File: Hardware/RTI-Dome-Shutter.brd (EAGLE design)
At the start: 80 x 71.1 mm, 42 parts, among them IC1 24AA128ST, IC5 74LVC245, IC6 74ABT245

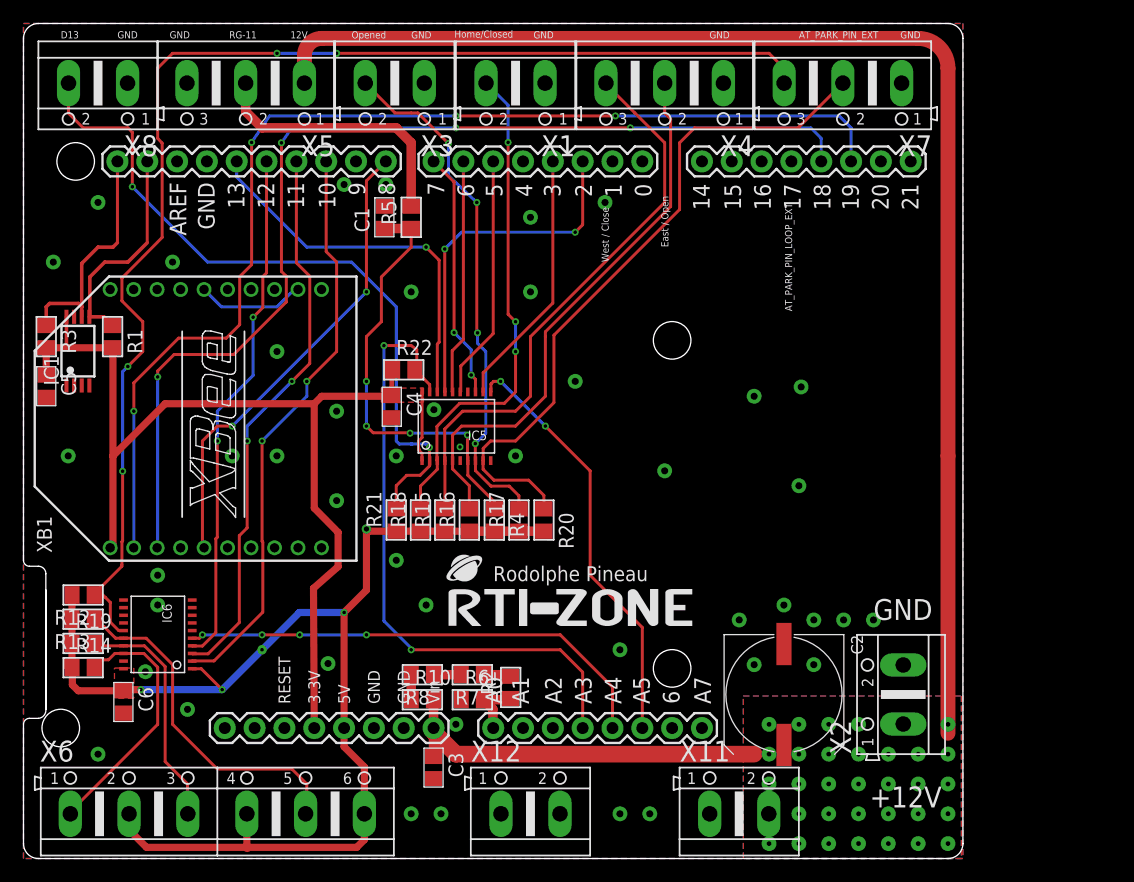
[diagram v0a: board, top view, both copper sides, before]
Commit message: Added powerpole to shutter shield
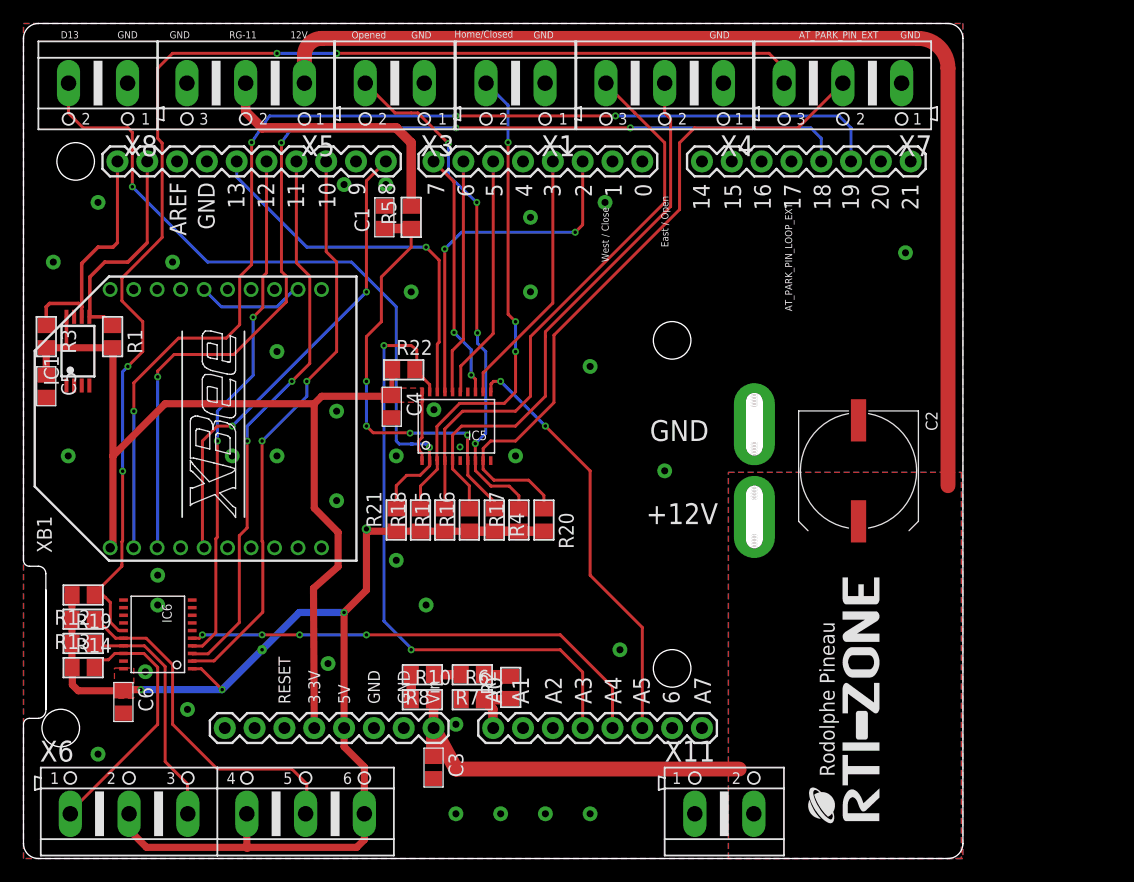
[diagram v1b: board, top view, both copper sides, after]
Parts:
- removed X12, X2: (no value), con-ptr500:AK500/2
- added J1: POWERPOLE_POWER45A, powerpoles:POWERPOLE_PAIR_45A
- moved U$4 40.3 mm to (72.9, 3.17), turned to 90 degrees
- moved C2 20.1 mm to (71.1, 33.0)
- moved X11 1.27 mm to (59.7, 3.81)
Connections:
- net +12V: now also J1.RED; no longer X2.1
- net GND: now also J1.BLACK; no longer X12.1, X12.2, X2.2
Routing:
- net +12V: track 148.7 -> 127.3 mm, vias 32 -> 0

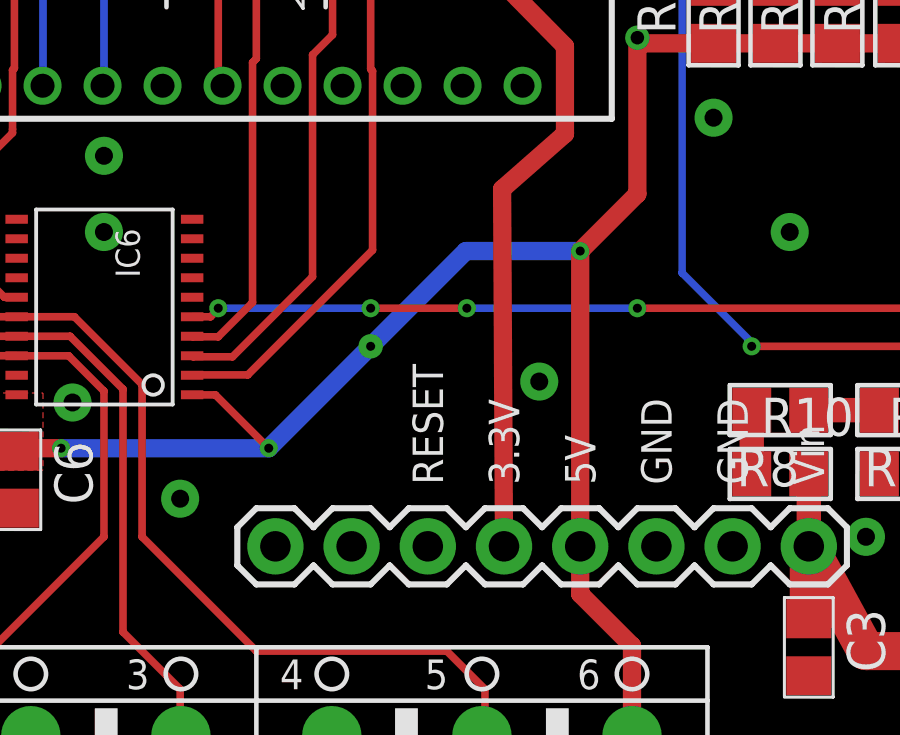
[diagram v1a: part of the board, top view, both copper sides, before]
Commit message: Adding MCP120 for power on reset.
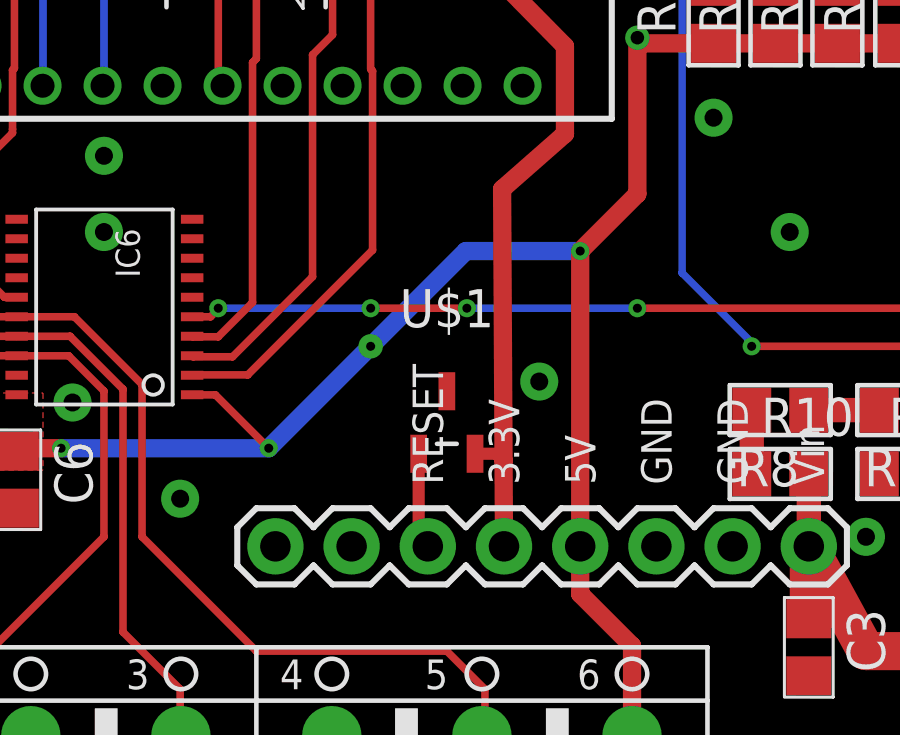
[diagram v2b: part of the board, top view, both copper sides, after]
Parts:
- added U$1: MCP120T-270I_TT, MCP120T-270I_TT:SOT95P237X112-3N
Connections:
- new net RESET: PCB1.RESET, U$1.1
- net 3.3V: now also U$1.2
- net GND: now also U$1.3
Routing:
- net RESET: track 0.00 -> 3.21 mm
- net 3.3V: track 91.5 -> 92.5 mm
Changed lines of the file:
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@@
 <element name="R22" library="rti" package="R0805" value="4.7K" x="32.385" y="41.62425"/>
 <element name="J1" library="powerpoles" package="POWERPOLE_PAIR_45A" value="POWERPOLE_POWER45A" x="62.23" y="33.02" rot="MR90"/>
+<element name="U$1" library="MCP120T-270I_TT" package="SOT95P237X112-3N" value="MCP120T-270I_TT" x="22.86" y="15.24">
+<attribute name="MANUFACTURER_PART_NUMBER" value="MCP120T-270I/TT" x="22.86" y="15.24" size="1.778" layer="27" display="off"/>
+<attribute name="MANUFACTURER_NAME" value="Microchip" x="22.86" y="15.24" size="1.778" layer="27" display="off"/>
+<attribute name="MOUSER_PART_NUMBER" value="579-MCP120T-270I/TT" x="22.86" y="15.24" size="1.778" layer="27" display="off"/>
+<attribute name="DESCRIPTION" value="Microcontroller Supervisory Circuit" x="22.86" y="15.24" size="1.778" layer="27" display="off"/>
+<attribute name="HEIGHT" value="mm" x="22.86" y="15.24" size="1.778" layer="27" display="off"/>
+<attribute name="MOUSER_PRICE-STOCK" value="https://www.mouser.co.uk/ProductDetail/Microchip-Technology/MCP120T-270I-TT?qs=JaP0%252BruNJH91Pwyk6aJdSA%3D%3D" x="22.86" y="15.24" size="1.778" layer="27" display="off"/>
+</element>
 </elements>
 <signals>
@@
 <via x="37.17925" y="35.052" extent="1-16" drill="0.3" diameter="0.254"/>
 <contactref element="J1" pad="BLACK"/>
+<contactref element="U$1" pad="3"/>
 <wire x1="62.25" y1="36.99" x2="62.23" y2="39.37" width="0" layer="19" extent="1-1"/>
 </signal>
@@
 <wire x1="7.62" y1="26.702" x2="7.383" y2="26.465" width="0.6096" layer="1"/>
 <contactref element="PCB1" pad="3.3V"/>
-<wire x1="24.765" y1="11.1125" x2="24.7015" y2="23.01875" width="0.6096" layer="1"/>
+<wire x1="24.765" y1="11.1125" x2="24.74974375" y2="13.97330625" width="0.6096" layer="1"/>
+<wire x1="24.74974375" y1="13.97330625" x2="24.7015" y2="23.01875" width="0.6096" layer="1"/>
 <wire x1="24.7015" y1="23.01875" x2="26.797" y2="24.86025" width="0.6096" layer="1"/>
 <wire x1="26.797" y1="24.86025" x2="26.797" y2="27.78125" width="0.6096" layer="1"/>
@@
 <wire x1="31.435" y1="41.62425" x2="31.369" y2="41.55825" width="0.4064" layer="1"/>
 <wire x1="31.369" y1="41.55825" x2="31.369" y2="39.431" width="0.4064" layer="1"/>
+<contactref element="U$1" pad="2"/>
+<wire x1="23.7998" y1="14.1986" x2="24.52445" y2="14.1986" width="0.4064" layer="1"/>
+<wire x1="24.52445" y1="14.1986" x2="24.74974375" y2="13.97330625" width="0.4064" layer="1"/>
 </signal>
 <signal name="RG-11-IN_5V">
@@
 <contactref element="IC5" pad="P$14"/>
 </signal>
+<signal name="RESET">
+<contactref element="PCB1" pad="RESET"/>
+<contactref element="U$1" pad="1"/>
+<wire x1="21.9202" y1="14.1986" x2="21.9202" y2="11.4173" width="0.4064" layer="1"/>
+<wire x1="21.9202" y1="11.4173" x2="22.225" y2="11.1125" width="0.4064" layer="1"/>
+</signal>
 </signals>

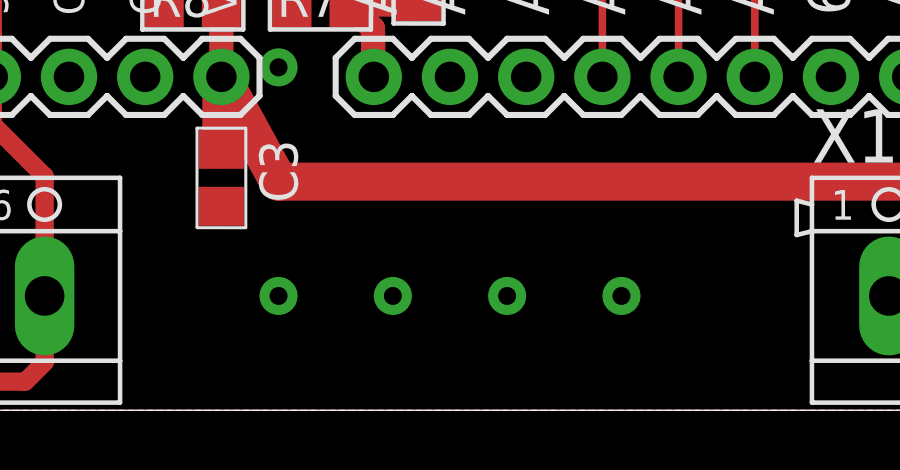
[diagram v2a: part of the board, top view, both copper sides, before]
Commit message: Redid the analog 3.3V on the ethernet shield
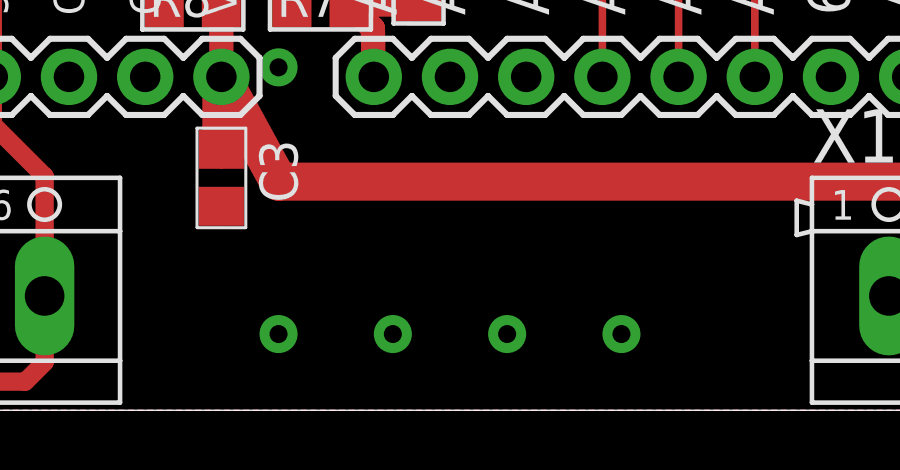
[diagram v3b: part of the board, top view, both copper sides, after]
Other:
- board text added: "Dome Shutter"
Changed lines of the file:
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@@
 <text x="3.175" y="69.85" size="0.6096" layer="21">D13</text>
 <text x="4.60375" y="68.61175" size="0.6096" layer="22" rot="MR0">D13</text>
+<text x="36.83" y="3.81" size="1.778" layer="51">Dome Shutter</text>
 </plain>
 <attributes>
@@
 <via x="6.35" y="8.89" extent="1-16" drill="0.6" diameter="1.27"/>
 <via x="10.38225" y="15.90675" extent="1-16" drill="0.6" diameter="1.27"/>
-<via x="36.83" y="3.81" extent="1-16" drill="0.6" diameter="1.27"/>
-<via x="40.64" y="3.81" extent="1-16" drill="0.6" diameter="1.27"/>
-<via x="44.45" y="3.81" extent="1-16" drill="0.6" diameter="1.27"/>
-<via x="48.26" y="3.81" extent="1-16" drill="0.6" diameter="1.27"/>
+<via x="36.83" y="2.54" extent="1-16" drill="0.6" diameter="1.27"/>
+<via x="40.64" y="2.54" extent="1-16" drill="0.6" diameter="1.27"/>
+<via x="44.45" y="2.54" extent="1-16" drill="0.6" diameter="1.27"/>
+<via x="48.26" y="2.54" extent="1-16" drill="0.6" diameter="1.27"/>
 <via x="2.54" y="50.8" extent="1-16" drill="0.6" diameter="1.27"/>
 <via x="6.35" y="55.88" extent="1-16" drill="0.6" diameter="1.27"/>

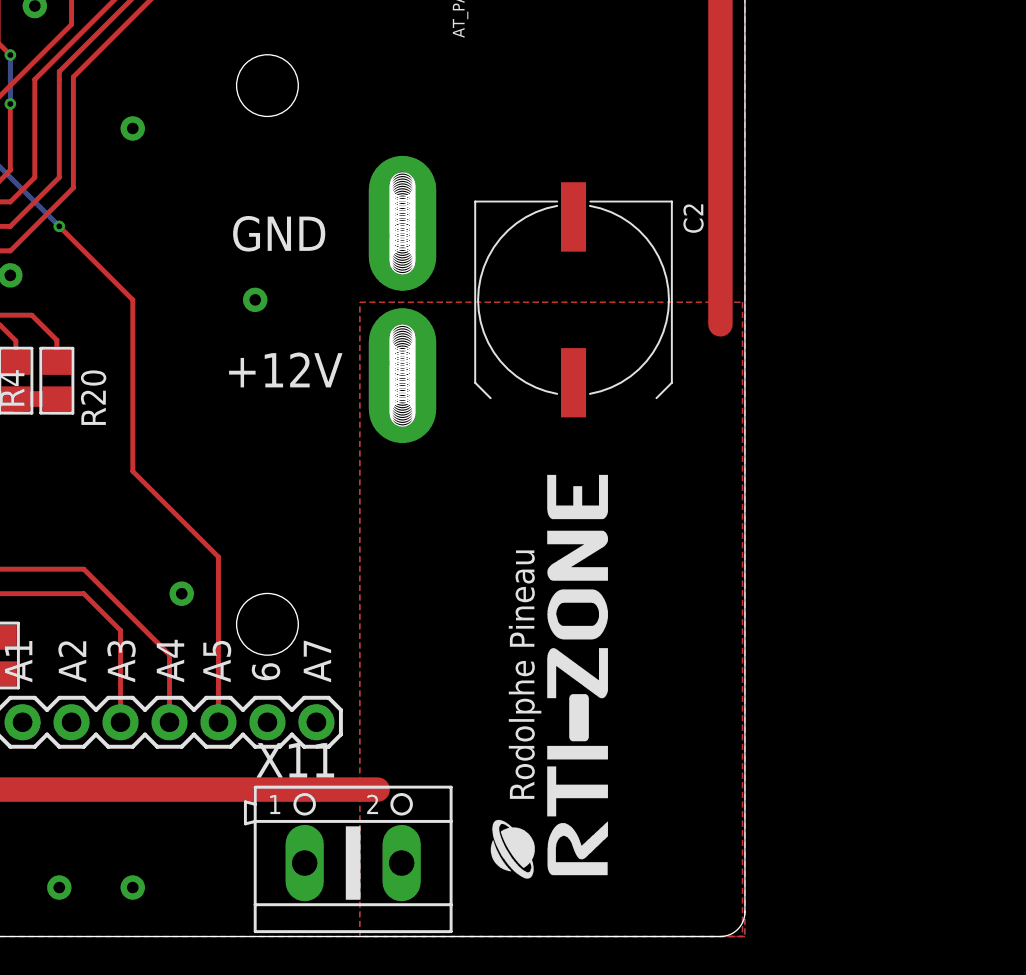
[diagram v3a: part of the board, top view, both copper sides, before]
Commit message: Fix some routing
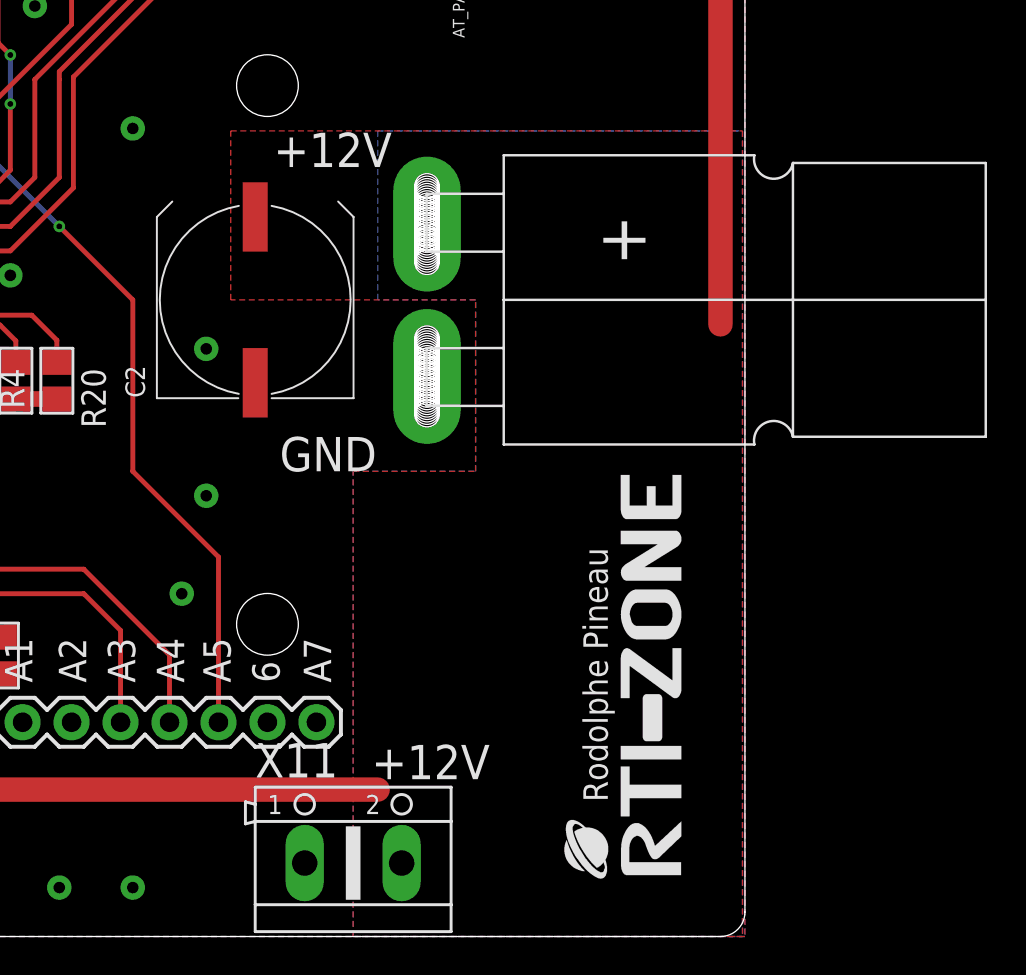
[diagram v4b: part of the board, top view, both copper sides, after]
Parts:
- moved C2 16.5 mm to (54.6, 33.0), turned to 90 degrees
- moved U$4 3.81 mm to (76.7, 3.17)
- moved J1 1.27 mm to (63.5, 33.0), flipped to the top, turned to 270 degrees
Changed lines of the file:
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@@
 <text x="57.15" y="69.88175" size="0.6096" layer="22" rot="MR0">East / Open</text>
 <text x="58.42" y="69.85" size="0.6096" layer="21">GND</text>
-<text x="53.34" y="35.56" size="1.778" layer="21">GND</text>
-<text x="53.0225" y="28.47975" size="1.778" layer="21">+12V</text>
+<text x="55.88" y="24.13" size="1.778" layer="21">GND</text>
+<text x="55.5625" y="39.90975" size="1.778" layer="21">+12V</text>
 <wire x1="1.905" y1="22.86" x2="1.905" y2="12.7" width="0" layer="20"/>
 <text x="36.703" y="69.9135" size="0.6096" layer="21">Home/Closed</text>
@@
 <text x="4.60375" y="68.61175" size="0.6096" layer="22" rot="MR0">D13</text>
 <text x="36.83" y="3.81" size="1.778" layer="51">Dome Shutter</text>
+<text x="60.6425" y="8.15975" size="1.778" layer="21">+12V</text>
 </plain>
 <attributes>
@@
 <element name="C1" library="rti" package="C0805" value="10uF" x="30.734" y="54.61" rot="R90"/>
 <element name="R5" library="rti" package="R0805" value="100" x="33.02" y="54.61" rot="R90"/>
-<element name="U$4" library="rti" package="LOGO_BIG" value="RTI-LOGO_BIG" x="72.898" y="3.175" rot="R90"/>
-<element name="C2" library="rti" package="UD-10X10_NICHICON" value="100uF" x="71.12" y="33.02" rot="R270"/>
+<element name="U$4" library="rti" package="LOGO_BIG" value="RTI-LOGO_BIG" x="76.708" y="3.175" rot="R90"/>
+<element name="C2" library="rti" package="UD-10X10_NICHICON" value="100uF" x="54.61" y="33.02" rot="R90"/>
 <element name="R13" library="rti" package="R0805" value="4.7K" x="5.08" y="20.3835" rot="R180"/>
 <element name="R14" library="rti" package="R0805" value="4.7K" x="5.08" y="16.256"/>
@@
 <element name="IC6" library="rti" package="TSSOP20" value="74ABT245" x="11.43" y="19.05" rot="R180"/>
 <element name="R22" library="rti" package="R0805" value="4.7K" x="32.385" y="41.62425"/>
-<element name="J1" library="powerpoles" package="POWERPOLE_PAIR_45A" value="POWERPOLE_POWER45A" x="62.23" y="33.02" rot="MR90"/>
+<element name="J1" library="powerpoles" package="POWERPOLE_PAIR_45A" value="POWERPOLE_POWER45A" x="63.5" y="33.02" rot="R270"/>
 <element name="U$1" library="MCP120T-270I_TT" package="SOT95P237X112-3N" value="MCP120T-270I_TT" x="22.86" y="15.24">
 <attribute name="MANUFACTURER_PART_NUMBER" value="MCP120T-270I/TT" x="22.86" y="15.24" size="1.778" layer="27" display="off"/>
@@
 <contactref element="C6" pad="2"/>
 <via x="11.43" y="21.59" extent="1-16" drill="0.6" diameter="1.27"/>
-<via x="62.23" y="39.37" extent="1-16" drill="0.6" diameter="1.27"/>
+<via x="52.07" y="22.86" extent="1-16" drill="0.6" diameter="1.27"/>
 <via x="50.8" y="17.78" extent="1-16" drill="0.6" diameter="1.27"/>
 <via x="34.29" y="21.59" extent="1-16" drill="0.6" diameter="1.27"/>
-<via x="54.61" y="33.02" extent="1-16" drill="0.6" diameter="1.27"/>
+<via x="52.07" y="30.48" extent="1-16" drill="0.6" diameter="1.27"/>
 <via x="43.18" y="54.61" extent="1-16" drill="0.6" diameter="1.27"/>
 <via x="34.95675" y="38.227" extent="1-16" drill="0.6" diameter="1.27"/>
@@
 <contactref element="J1" pad="BLACK"/>
 <contactref element="U$1" pad="3"/>
-<wire x1="62.25" y1="36.99" x2="62.23" y2="39.37" width="0" layer="19" extent="1-1"/>
 </signal>
 <signal name="+12V" class="1">
@@
 <contactref element="C2" pad="+"/>
 <polygon width="0.3048" layer="1" thermals="no">
-<vertex x="60.04" y="32.893"/>
-<vertex x="79.883" y="32.893"/>
+<vertex x="53.34" y="41.783"/>
+<vertex x="79.883" y="41.783"/>
 <vertex x="79.883" y="0"/>
-<vertex x="60.04" y="0"/>
+<vertex x="59.69" y="0"/>
+<vertex x="59.69" y="24.13"/>
+<vertex x="66.04" y="24.13"/>
+<vertex x="66.04" y="33.02"/>
+<vertex x="53.34" y="33.02"/>
 </polygon>
 <contactref element="R10" pad="2"/>
@@
 <wire x1="25.4" y1="69.85" x2="23.9268" y2="68.3768" width="1.27" layer="1" curve="90"/>
 <polygon width="0.254" layer="16" thermals="no">
-<vertex x="60.04" y="32.893"/>
-<vertex x="79.883" y="32.893"/>
+<vertex x="60.96" y="41.783"/>
+<vertex x="79.883" y="41.783"/>
 <vertex x="79.883" y="0"/>
-<vertex x="60.04" y="0"/>
+<vertex x="59.69" y="0"/>
+<vertex x="59.69" y="24.13"/>
+<vertex x="66.04" y="24.13"/>
+<vertex x="66.04" y="33.02"/>
+<vertex x="60.96" y="33.02"/>
 </polygon>
 <wire x1="34.9225" y1="13.5255" x2="34.925" y2="13.5255" width="0.8128" layer="1"/>
@@
 <wire x1="36.83" y1="7.62" x2="60.96" y2="7.62" width="1.27" layer="1"/>
 <wire x1="34.925" y1="8.697" x2="34.925" y2="11.1125" width="1.27" layer="1"/>
+<wire x1="63.52" y1="37.32" x2="63.52" y2="36.95" width="2.54" layer="1"/>
 </signal>
 <signal name="SHUTTER_OPENED">
